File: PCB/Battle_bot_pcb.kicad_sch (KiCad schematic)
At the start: 0 parts

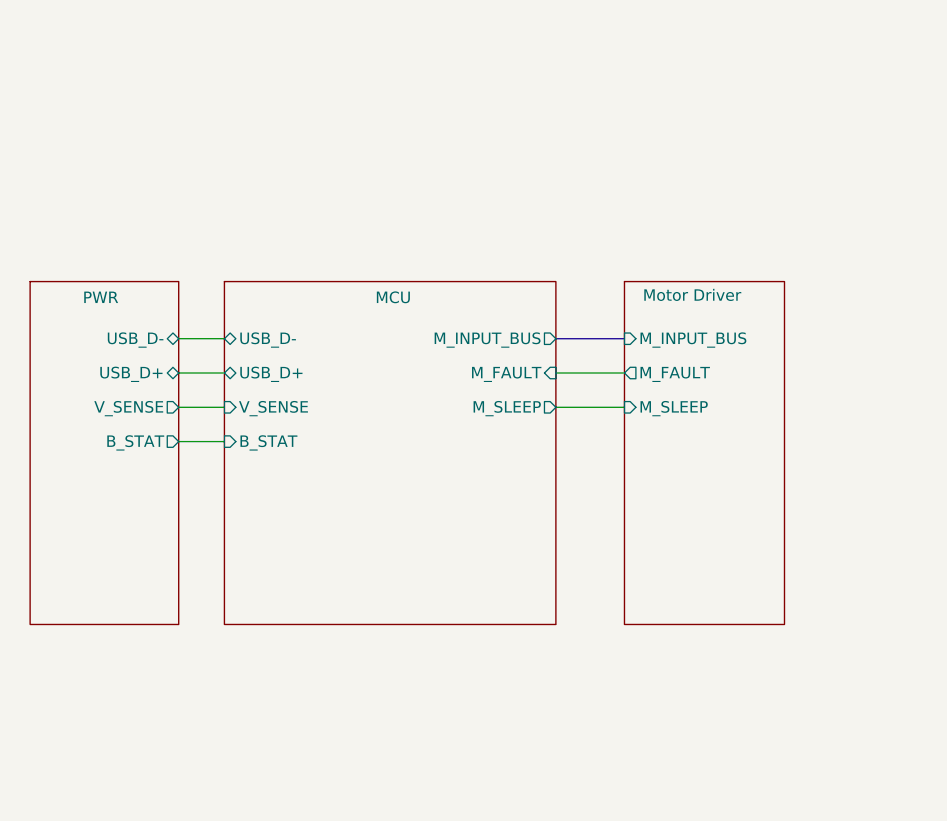
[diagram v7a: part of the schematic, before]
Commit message: Added branch for integraed BLDC motor control
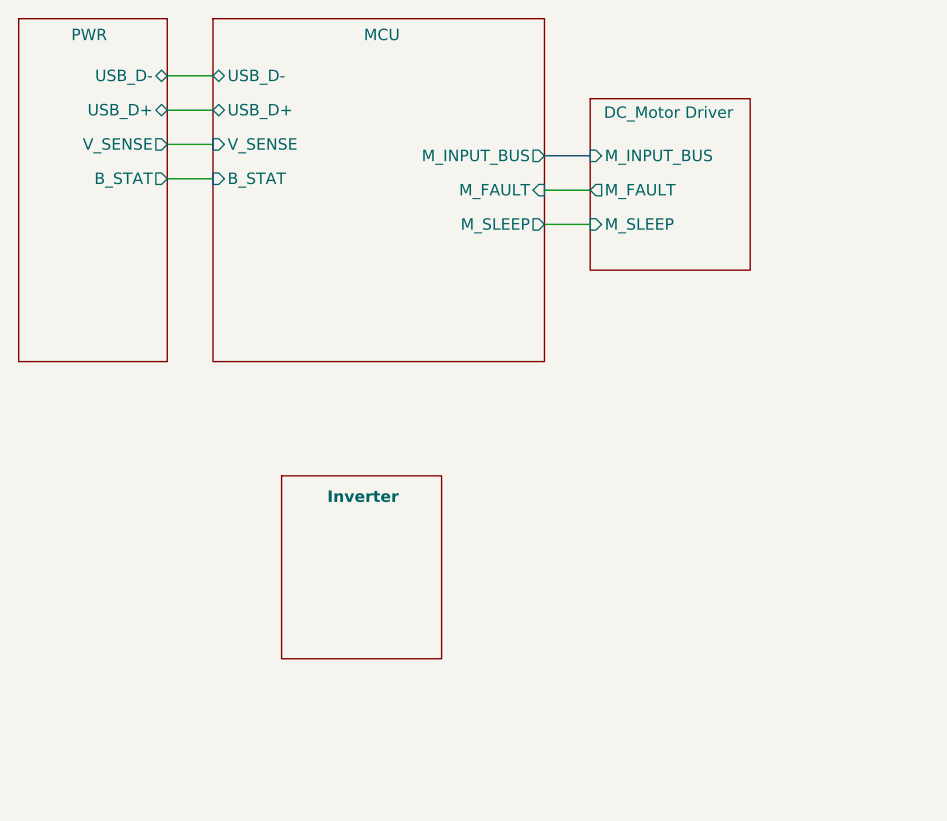
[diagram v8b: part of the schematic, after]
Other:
- sheet Motor Driver renamed DC_Motor Driver
- added sheet Inverter (inverter.kicad_sch)
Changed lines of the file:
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@@
 (kicad_sch
-	(version 20231120)
+	(version 20250114)
 	(generator "eeschema")
-	(generator_version "8.0")
+	(generator_version "9.0")
 	(paper "A4")
-	(wire
-		(pts
-			(xy 162.56 90.17) (xy 170.18 90.17)
-		)
-		(stroke
-			(width 0)
-			(type default)
-		)
-	)
-	(bus
-		(pts
-			(xy 162.56 86.36) (xy 170.18 86.36)
-		)
-		(stroke
-			(width 0)
-			(type default)
-		)
-	)
-	(wire
-		(pts
-			(xy 120.65 86.36) (xy 125.73 86.36)
-		)
-		(stroke
-			(width 0)
-			(type default)
-		)
-	)
-	(wire
-		(pts
-			(xy 120.65 97.79) (xy 125.73 97.79)
-		)
-		(stroke
-			(width 0)
-			(type default)
-		)
-	)
-	(wire
-		(pts
-			(xy 120.65 90.17) (xy 125.73 90.17)
-		)
-		(stroke
-			(width 0)
-			(type default)
-		)
-	)
-	(wire
-		(pts
-			(xy 120.65 93.98) (xy 125.73 93.98)
-		)
-		(stroke
-			(width 0)
-			(type default)
-		)
-	)
-	(wire
-		(pts
-			(xy 162.56 93.98) (xy 170.18 93.98)
-		)
-		(stroke
-			(width 0)
-			(type default)
-		)
-	)
 	(text "Functional Blocks"
 		(exclude_from_sim no)
@@
 		)
 	)
+	(wire
+		(pts
+			(xy 161.29 69.85) (xy 166.37 69.85)
+		)
+		(stroke
+			(width 0)
+			(type default)
+		)
+	)
+	(bus
+		(pts
+			(xy 161.29 66.04) (xy 166.37 66.04)
+		)
+		(stroke
+			(width 0)
+			(type default)
+		)
+	)
+	(wire
+		(pts
+			(xy 119.38 57.15) (xy 124.46 57.15)
+		)
+		(stroke
+			(width 0)
+			(type default)
+		)
+	)
+	(wire
+		(pts
+			(xy 119.38 68.58) (xy 124.46 68.58)
+		)
+		(stroke
+			(width 0)
+			(type default)
+		)
+	)
+	(wire
+		(pts
+			(xy 119.38 60.96) (xy 124.46 60.96)
+		)
+		(stroke
+			(width 0)
+			(type default)
+		)
+	)
+	(wire
+		(pts
+			(xy 119.38 64.77) (xy 124.46 64.77)
+		)
+		(stroke
+			(width 0)
+			(type default)
+		)
+	)
+	(wire
+		(pts
+			(xy 161.29 73.66) (xy 166.37 73.66)
+		)
+		(stroke
+			(width 0)
+			(type default)
+		)
+	)
 	(sheet
-		(at 104.14 80.01)
-		(size 16.51 38.1)
+		(at 132.08 101.6)
+		(size 17.78 20.32)
+		(exclude_from_sim no)
+		(in_bom yes)
+		(on_board yes)
+		(dnp no)
 		(stroke
 			(width 0.1524)
@@
 			(color 200 200 200 1.0000)
 		)
-		(property "Sheetname" "PWR"
-			(at 109.982 82.55 0)
-			(effects
-				(font
-					(size 1.27 1.27)
+		(property "Sheetname" "Inverter"
+			(at 137.16 104.648 0)
+			(effects
+				(font
+					(size 1.27 1.27)
+					(thickness 0.254)
+					(bold yes)
 				)
 				(justify left bottom)
 			)
 		)
-		(property "Sheetfile" "pwr.kicad_sch"
-			(at 104.14 118.6946 0)
+		(property "Sheetfile" "inverter.kicad_sch"
+			(at 132.08 122.5046 0)
 			(effects
 				(font
@@
 			)
 		)
+		(instances
+			(project "Battle_bot_pcb"
+				(path "/d6203762-4d2e-4b90-86d1-ca295813f2e5"
+					(page "5")
+				)
+			)
+		)
+	)
+	(sheet
+		(at 102.87 50.8)
+		(size 16.51 38.1)
+		(exclude_from_sim no)
+		(in_bom yes)
+		(on_board yes)
+		(dnp no)
+		(stroke
+			(width 0.1524)
+			(type solid)
+		)
+		(fill
+			(color 200 200 200 1.0000)
+		)
+		(property "Sheetname" "PWR"
+			(at 108.712 53.34 0)
+			(effects
+				(font
+					(size 1.27 1.27)
+				)
+				(justify left bottom)
+			)
+		)
+		(property "Sheetfile" "pwr.kicad_sch"
+			(at 102.87 89.4846 0)
+			(effects
+				(font
+					(size 1.27 1.27)
+				)
+				(justify left top)
+				(hide yes)
+			)
+		)
 		(pin "USB_D-" bidirectional
-			(at 120.65 86.36 0)
+			(at 119.38 57.15 0)
 			(effects
 				(font
@@
 		)
 		(pin "USB_D+" bidirectional
-			(at 120.65 90.17 0)
+			(at 119.38 60.96 0)
 			(effects
 				(font
@@
 		)
 		(pin "B_STAT" output
-			(at 120.65 97.79 0)
+			(at 119.38 68.58 0)
 			(effects
 				(font
@@
 		)
 		(pin "V_SENSE" output
-			(at 120.65 93.98 0)
+			(at 119.38 64.77 0)
 			(effects
 				(font
@@
 	)
 	(sheet
-		(at 125.73 80.01)
+		(at 124.46 50.8)
 		(size 36.83 38.1)
+		(exclude_from_sim no)
+		(in_bom yes)
+		(on_board yes)
+		(dnp no)
 		(stroke
 			(width 0.1524)
@@
 		)
 		(property "Sheetname" "MCU"
-			(at 142.494 82.55 0)
+			(at 141.224 53.34 0)
 			(effects
 				(font
@@
 		)
 		(property "Sheetfile" "mcu.kicad_sch"
-			(at 125.73 118.6946 0)
+			(at 124.46 89.4846 0)
 			(effects
 				(font
@@
 		)
 		(pin "USB_D+" bidirectional
-			(at 125.73 90.17 180)
+			(at 124.46 60.96 180)
 			(effects
 				(font
@@
 		)
 		(pin "USB_D-" bidirectional
-			(at 125.73 86.36 180)
+			(at 124.46 57.15 180)
 			(effects
 				(font
@@
 		)
 		(pin "M_INPUT_BUS" output
-			(at 162.56 86.36 0)
+			(at 161.29 66.04 0)
 			(effects
 				(font
@@
 		)
 		(pin "V_SENSE" input
-			(at 125.73 93.98 180)
+			(at 124.46 64.77 180)
 			(effects
 				(font
@@
 		)
 		(pin "M_FAULT" input
-			(at 162.56 90.17 0)
+			(at 161.29 69.85 0)
 			(effects
 				(font
@@
 		)
 		(pin "B_STAT" input
-			(at 125.73 97.79 180)
+			(at 124.46 68.58 180)
 			(effects
 				(font
@@
 		)
 		(pin "M_SLEEP" output
-			(at 162.56 93.98 0)
+			(at 161.29 73.66 0)
 			(effects
 				(font
@@
 	)
 	(sheet
-		(at 170.18 80.01)
-		(size 17.78 38.1)
+		(at 166.37 59.69)
+		(size 17.78 19.05)
+		(exclude_from_sim no)
+		(in_bom yes)
+		(on_board yes)
+		(dnp no)
 		(stroke
 			(width 0.1524)
@@
 			(color 201 201 201 1.0000)
 		)
-		(property "Sheetname" "Motor Driver"
-			(at 172.212 82.296 0)
+		(property "Sheetname" "DC_Motor Driver"
+			(at 167.894 61.976 0)
 			(effects
 				(font
@@
 		)
 		(property "Sheetfile" "io.kicad_sch"
-			(at 170.18 117.4246 0)
+			(at 166.37 97.1046 0)
 			(effects
 				(font
@@
 		)
 		(pin "M_INPUT_BUS" input
-			(at 170.18 86.36 180)
+			(at 166.37 66.04 180)
 			(effects
 				(font
@@
 		)
 		(pin "M_FAULT" output
-			(at 170.18 90.17 180)
+			(at 166.37 69.85 180)
 			(effects
 				(font
@@
 		)
 		(pin "M_SLEEP" input
-			(at 170.18 93.98 180)
+			(at 166.37 73.66 180)
 			(effects
 				(font
@@
 		)
 	)
+	(embedded_fonts no)
 )
